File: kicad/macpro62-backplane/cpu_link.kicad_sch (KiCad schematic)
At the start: 0 parts

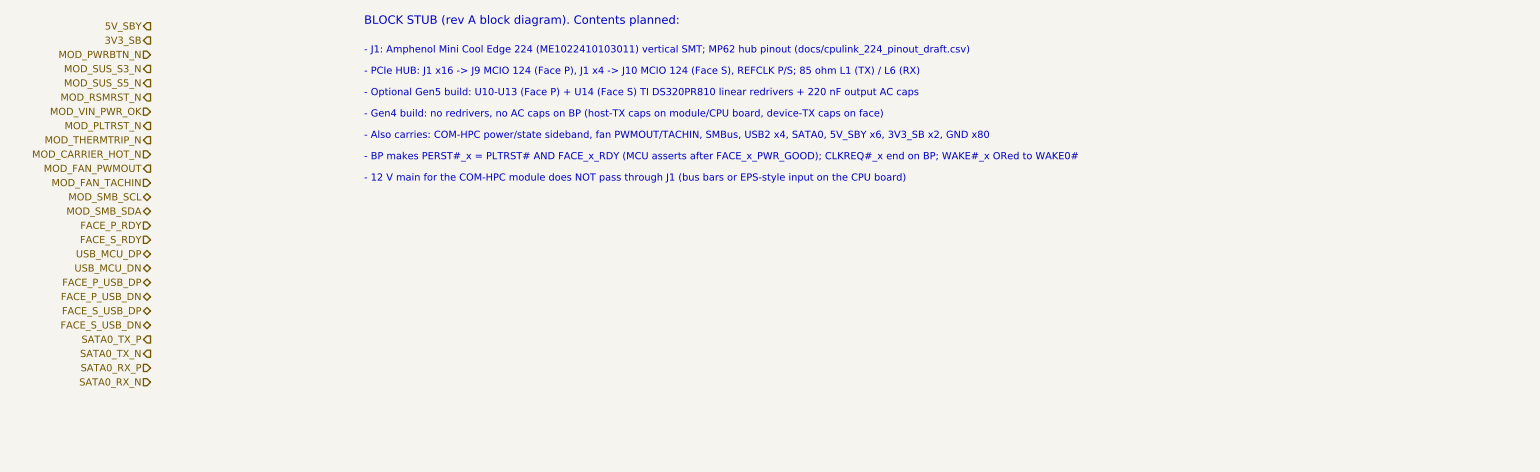
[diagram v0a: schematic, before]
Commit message: Cross-board compatibility audit: interface control doc, CR-BP-1 applied, J2/J3 row-swap pinouts, 15-pin face AUX, fan header removed from backplane, CPU board i226/BT1 cleanup
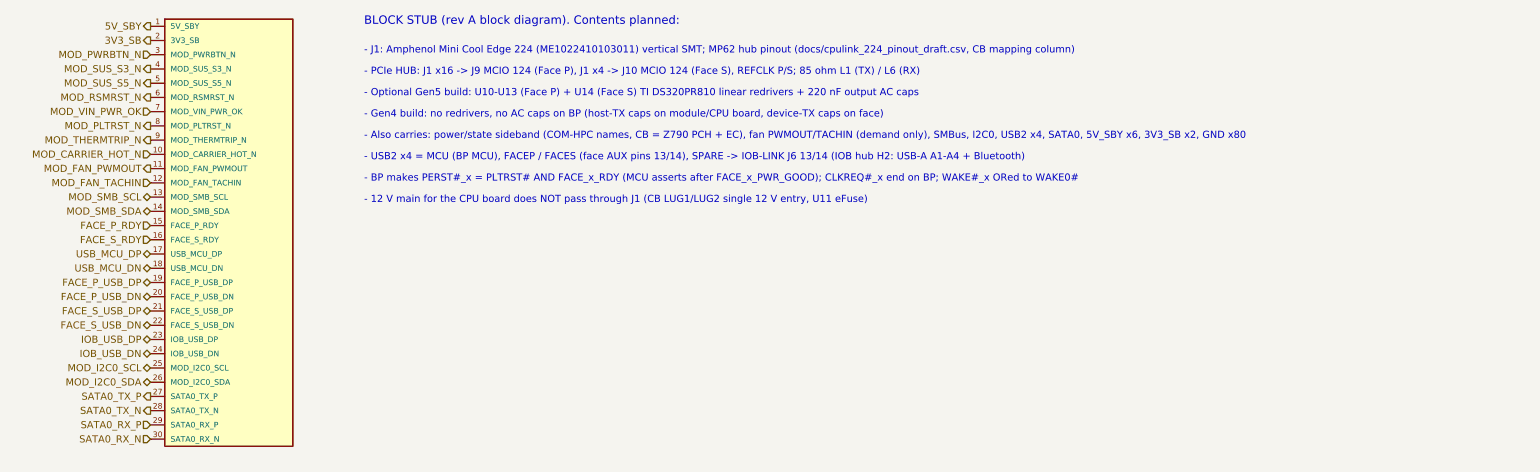
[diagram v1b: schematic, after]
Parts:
- added #BLK5: STUB_CPU_LINK, symbol MP62:STUB_CPU_LINK
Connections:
- net 3V3_SB: now also #BLK5.2 (3V3_SB)
- net 5V_SBY: now also #BLK5.1 (5V_SBY)
- net FACE_P_RDY: now also #BLK5.15 (FACE_P_RDY)
- net FACE_P_USB_DN: now also #BLK5.20 (FACE_P_USB_DN)
- net FACE_P_USB_DP: now also #BLK5.19 (FACE_P_USB_DP)
- net FACE_S_RDY: now also #BLK5.16 (FACE_S_RDY)
- net FACE_S_USB_DN: now also #BLK5.22 (FACE_S_USB_DN)
- net FACE_S_USB_DP: now also #BLK5.21 (FACE_S_USB_DP)
- net MOD_CARRIER_HOT_N: now also #BLK5.10 (MOD_CARRIER_HOT_N)
- net MOD_FAN_PWMOUT: now also #BLK5.11 (MOD_FAN_PWMOUT)
- net MOD_FAN_TACHIN: now also #BLK5.12 (MOD_FAN_TACHIN)
- net MOD_PLTRST_N: now also #BLK5.8 (MOD_PLTRST_N)
- net MOD_PWRBTN_N: now also #BLK5.3 (MOD_PWRBTN_N)
- net MOD_RSMRST_N: now also #BLK5.6 (MOD_RSMRST_N)
- net MOD_SMB_SCL: now also #BLK5.13 (MOD_SMB_SCL)
- net MOD_SMB_SDA: now also #BLK5.14 (MOD_SMB_SDA)
- net MOD_SUS_S3_N: now also #BLK5.4 (MOD_SUS_S3_N)
- net MOD_SUS_S5_N: now also #BLK5.5 (MOD_SUS_S5_N)
- net MOD_THERMTRIP_N: now also #BLK5.9 (MOD_THERMTRIP_N)
- net MOD_VIN_PWR_OK: now also #BLK5.7 (MOD_VIN_PWR_OK)
- net SATA0_RX_N: now also #BLK5.30 (SATA0_RX_N)
- net SATA0_RX_P: now also #BLK5.29 (SATA0_RX_P)
- net SATA0_TX_N: now also #BLK5.28 (SATA0_TX_N)
- net SATA0_TX_P: now also #BLK5.27 (SATA0_TX_P)
- net USB_MCU_DN: now also #BLK5.18 (USB_MCU_DN)
- net USB_MCU_DP: now also #BLK5.17 (USB_MCU_DP)
- new net IOB_USB_DN: #BLK5.24 (IOB_USB_DN)
- new net IOB_USB_DP: #BLK5.23 (IOB_USB_DP)
- new net MOD_I2C0_SCL: #BLK5.25 (MOD_I2C0_SCL)
- new net MOD_I2C0_SDA: #BLK5.26 (MOD_I2C0_SDA)
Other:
- note added: "- 12 V main for the CPU board does NOT pass through J1 (CB LUG1/LUG2 single 12 V entry, U11 eFuse)"
- note added: "- Also carries: power/state sideband (COM-HPC names, CB = Z790 PCH + EC), fan PWMOUT/TACHIN (demand only), SMBus, I2C0, USB2 x4, SATA0, 5V_SBY x6, 3V3_SB x2, GND x80"
- note added: "- J1: Amphenol Mini Cool Edge 224 (ME1022410103011) vertical SMT; MP62 hub pinout (docs/cpulink_224_pinout_draft.csv, CB mapping column)"
- note added: "- USB2 x4 = MCU (BP MCU), FACEP / FACES (face AUX pins 13/14), SPARE -> IOB-LINK J6 13/14 (IOB hub H2: USB-A A1-A4 + Bluetooth)"
- note removed: "- 12 V main for the COM-HPC module does NOT pass through J1 (bus bars or EPS-style input on the CPU board)"
- note removed: "- Also carries: COM-HPC power/state sideband, fan PWMOUT/TACHIN, SMBus, USB2 x4, SATA0, 5V_SBY x6, 3V3_SB x2, GND x80"
- note removed: "- J1: Amphenol Mini Cool Edge 224 (ME1022410103011) vertical SMT; MP62 hub pinout (docs/cpulink_224_pinout_draft.csv)"
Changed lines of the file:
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@@
 	(title_block
 		(title "MP62 backplane: CPU board link (J1 CPU-LINK card edge)")
-		(date "2026-10-01")
-		(rev "A-bd1")
-		(comment 1 "Block stub: hierarchical labels only, circuit TBD")
+		(date "2026-10-02")
+		(rev "A-bd2")
+		(comment 1 "Block stub: hierarchical labels + one non-BOM stub symbol (#BLKn, passive pins) so ERC sees the nets; circuit TBD")
 	)
 	(hierarchical_label "5V_SBY"
@@
 		(effects (font (size 1.27 1.27)) (justify right))
 	)
+	(hierarchical_label "IOB_USB_DP"
+		(shape bidirectional)
+		(at 38.1 86.36 180)
+		(effects (font (size 1.27 1.27)) (justify right))
+	)
+	(hierarchical_label "IOB_USB_DN"
+		(shape bidirectional)
+		(at 38.1 88.90 180)
+		(effects (font (size 1.27 1.27)) (justify right))
+	)
+	(hierarchical_label "MOD_I2C0_SCL"
+		(shape bidirectional)
+		(at 38.1 91.44 180)
+		(effects (font (size 1.27 1.27)) (justify right))
+	)
+	(hierarchical_label "MOD_I2C0_SDA"
+		(shape bidirectional)
+		(at 38.1 93.98 180)
+		(effects (font (size 1.27 1.27)) (justify right))
+	)
 	(hierarchical_label "SATA0_TX_P"
 		(shape output)
-		(at 38.1 86.36 180)
+		(at 38.1 96.52 180)
 		(effects (font (size 1.27 1.27)) (justify right))
 	)
 	(hierarchical_label "SATA0_TX_N"
 		(shape output)
-		(at 38.1 88.90 180)
+		(at 38.1 99.06 180)
 		(effects (font (size 1.27 1.27)) (justify right))
 	)
 	(hierarchical_label "SATA0_RX_P"
 		(shape input)
-		(at 38.1 91.44 180)
+		(at 38.1 101.60 180)
 		(effects (font (size 1.27 1.27)) (justify right))
 	)
 	(hierarchical_label "SATA0_RX_N"
 		(shape input)
-		(at 38.1 93.98 180)
-		(effects (font (size 1.27 1.27)) (justify right))
+		(at 38.1 104.14 180)
+		(effects (font (size 1.27 1.27)) (justify right))
+	)
+	(symbol
+		(lib_id "MP62:STUB_CPU_LINK")
+		(at 38.1 30.48 0)
+		(unit 1)
+		(exclude_from_sim yes)
+		(in_bom no)
+		(on_board no)
+		(dnp no)
+		(property "Reference" "#BLK5"
+			(at 40.64 27.94 0)
+			(effects (font (size 1.27 1.27)) (justify left) (hide yes))
+		)
+		(property "Value" "STUB_CPU_LINK"
+			(at 40.64 26.67 0)
+			(effects (font (size 1.27 1.27)) (justify left) (hide yes))
+		)
+		(pin "1"
+		)
+		(pin "2"
+		)
+		(pin "3"
+		)
+		(pin "4"
+		)
+		(pin "5"
+		)
+		(pin "6"
+		)
+		(pin "7"
+		)
+		(pin "8"
+		)
+		(pin "9"
+		)
+		(pin "10"
+		)
+		(pin "11"
+		)
+		(pin "12"
+		)
+		(pin "13"
+		)
+		(pin "14"
+		)
+		(pin "15"
+		)
+		(pin "16"
+		)
+		(pin "17"
+		)
+		(pin "18"
+		)
+		(pin "19"
+		)
+		(pin "20"
+		)
+		(pin "21"
+		)
+		(pin "22"
+		)
+		(pin "23"
+		)
+		(pin "24"
+		)
+		(pin "25"
+		)
+		(pin "26"
+		)
+		(pin "27"
+		)
+		(pin "28"
+		)
+		(pin "29"
+		)
+		(pin "30"
+		)
+		(instances
+			(project "backplane"
+				(path "/6a1c2d3e-0000-4000-8000-000000000062/f1a0d997-9be8-4b41-9317-5f875cd4202e"
+					(reference "#BLK5")
+					(unit 1)
+				)
+			)
+		)
 	)
 	(text "BLOCK STUB (rev A block diagram). Contents planned:"
@@
 		(effects (font (size 1.5 1.5)) (justify left bottom))
 	)
-	(text "- J1: Amphenol Mini Cool Edge 224 (ME1022410103011) vertical SMT; MP62 hub pinout (docs/cpulink_224_pinout_draft.csv)"
+	(text "- J1: Amphenol Mini Cool Edge 224 (ME1022410103011) vertical SMT; MP62 hub pinout (docs/cpulink_224_pinout_draft.csv, CB mapping column)"
 		(exclude_from_sim no)
 		(at 76.20 35.56 0)
@@
 		(effects (font (size 1.27 1.27)) (justify left bottom))
 	)
-	(text "- Also carries: COM-HPC power/state sideband, fan PWMOUT/TACHIN, SMBus, USB2 x4, SATA0, 5V_SBY x6, 3V3_SB x2, GND x80"
+	(text "- Also carries: power/state sideband (COM-HPC names, CB = Z790 PCH + EC), fan PWMOUT/TACHIN (demand only), SMBus, I2C0, USB2 x4, SATA0, 5V_SBY x6, 3V3_SB x2, GND x80"
 		(exclude_from_sim no)
 		(at 76.20 50.80 0)
 		(effects (font (size 1.27 1.27)) (justify left bottom))
 	)
+	(text "- USB2 x4 = MCU (BP MCU), FACEP / FACES (face AUX pins 13/14), SPARE -> IOB-LINK J6 13/14 (IOB hub H2: USB-A A1-A4 + Bluetooth)"
+		(exclude_from_sim no)
+		(at 76.20 54.61 0)
+		(effects (font (size 1.27 1.27)) (justify left bottom))
+	)
 	(text "- BP makes PERST#_x = PLTRST# AND FACE_x_RDY (MCU asserts after FACE_x_PWR_GOOD); CLKREQ#_x end on BP; WAKE#_x ORed to WAKE0#"
 		(exclude_from_sim no)
-		(at 76.20 54.61 0)
-		(effects (font (size 1.27 1.27)) (justify left bottom))
-	)
-	(text "- 12 V main for the COM-HPC module does NOT pass through J1 (bus bars or EPS-style input on the CPU board)"
-		(exclude_from_sim no)
 		(at 76.20 58.42 0)
 		(effects (font (size 1.27 1.27)) (justify left bottom))
 	)
+	(text "- 12 V main for the CPU board does NOT pass through J1 (CB LUG1/LUG2 single 12 V entry, U11 eFuse)"
+		(exclude_from_sim no)
+		(at 76.20 62.23 0)
+		(effects (font (size 1.27 1.27)) (justify left bottom))
+	)

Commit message: ICD rev 2: 45 deg faces, 445 W ceiling + live power target (INA228 telemetry), ribbon MCIO jog cables, BT on S0, fan fail-safe, port-module I2C map
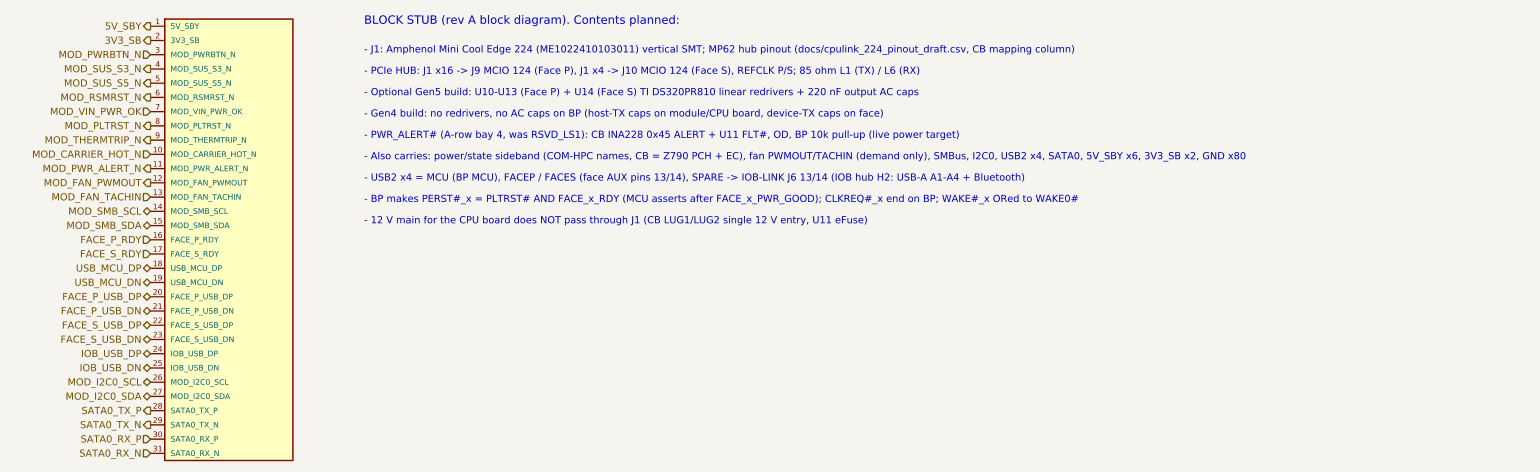
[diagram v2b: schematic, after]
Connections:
- net FACE_P_RDY: now also #BLK5.16 (FACE_P_RDY); no longer #BLK5.15 (FACE_P_RDY)
- net FACE_P_USB_DN: now also #BLK5.21 (FACE_P_USB_DN); no longer #BLK5.20 (FACE_P_USB_DN)
- net FACE_P_USB_DP: now also #BLK5.20 (FACE_P_USB_DP); no longer #BLK5.19 (FACE_P_USB_DP)
- net FACE_S_RDY: now also #BLK5.17 (FACE_S_RDY); no longer #BLK5.16 (FACE_S_RDY)
- net FACE_S_USB_DN: now also #BLK5.23 (FACE_S_USB_DN); no longer #BLK5.22 (FACE_S_USB_DN)
- net FACE_S_USB_DP: now also #BLK5.22 (FACE_S_USB_DP); no longer #BLK5.21 (FACE_S_USB_DP)
- net IOB_USB_DN: now also #BLK5.25 (IOB_USB_DN); no longer #BLK5.24 (IOB_USB_DN)
- net IOB_USB_DP: now also #BLK5.24 (IOB_USB_DP); no longer #BLK5.23 (IOB_USB_DP)
- net MOD_FAN_PWMOUT: now also #BLK5.12 (MOD_FAN_PWMOUT); no longer #BLK5.11 (MOD_FAN_PWMOUT)
- net MOD_FAN_TACHIN: now also #BLK5.13 (MOD_FAN_TACHIN); no longer #BLK5.12 (MOD_FAN_TACHIN)
- net MOD_I2C0_SCL: now also #BLK5.26 (MOD_I2C0_SCL); no longer #BLK5.25 (MOD_I2C0_SCL)
- net MOD_I2C0_SDA: now also #BLK5.27 (MOD_I2C0_SDA); no longer #BLK5.26 (MOD_I2C0_SDA)
- net MOD_SMB_SCL: now also #BLK5.14 (MOD_SMB_SCL); no longer #BLK5.13 (MOD_SMB_SCL)
- net MOD_SMB_SDA: now also #BLK5.15 (MOD_SMB_SDA); no longer #BLK5.14 (MOD_SMB_SDA)
- net SATA0_RX_N: now also #BLK5.31 (SATA0_RX_N); no longer #BLK5.30 (SATA0_RX_N)
- net SATA0_RX_P: now also #BLK5.30 (SATA0_RX_P); no longer #BLK5.29 (SATA0_RX_P)
- net SATA0_TX_N: now also #BLK5.29 (SATA0_TX_N); no longer #BLK5.28 (SATA0_TX_N)
- net SATA0_TX_P: now also #BLK5.28 (SATA0_TX_P); no longer #BLK5.27 (SATA0_TX_P)
- net USB_MCU_DN: now also #BLK5.19 (USB_MCU_DN); no longer #BLK5.18 (USB_MCU_DN)
- net USB_MCU_DP: now also #BLK5.18 (USB_MCU_DP); no longer #BLK5.17 (USB_MCU_DP)
- new net MOD_PWR_ALERT_N: #BLK5.11 (MOD_PWR_ALERT_N)
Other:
- note added: "- PWR_ALERT# (A-row bay 4, was RSVD_LS1): CB INA228 0x45 ALERT + U11 FLT#, OD, BP 10k pull-up (live power target)"
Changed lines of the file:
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@@
+		(effects (font (size 1.27 1.27)) (justify right))
+	)
+	(hierarchical_label "MOD_PWR_ALERT_N"
+		(shape output)
+		(at 38.1 55.88 180)
 		(effects (font (size 1.27 1.27)) (justify right))
 	)
 	(hierarchical_label "MOD_FAN_PWMOUT"
 		(shape output)
-		(at 38.1 55.88 180)
+		(at 38.1 58.42 180)
 		(effects (font (size 1.27 1.27)) (justify right))
 	)
 	(hierarchical_label "MOD_FAN_TACHIN"
 		(shape input)
-		(at 38.1 58.42 180)
+		(at 38.1 60.96 180)
 		(effects (font (size 1.27 1.27)) (justify right))
 	)
 	(hierarchical_label "MOD_SMB_SCL"
 		(shape bidirectional)
-		(at 38.1 60.96 180)
+		(at 38.1 63.50 180)
 		(effects (font (size 1.27 1.27)) (justify right))
 	)
 	(hierarchical_label "MOD_SMB_SDA"
 		(shape bidirectional)
-		(at 38.1 63.50 180)
+		(at 38.1 66.04 180)
 		(effects (font (size 1.27 1.27)) (justify right))
 	)
 	(hierarchical_label "FACE_P_RDY"
 		(shape input)
-		(at 38.1 66.04 180)
+		(at 38.1 68.58 180)
 		(effects (font (size 1.27 1.27)) (justify right))
 	)
 	(hierarchical_label "FACE_S_RDY"
 		(shape input)
-		(at 38.1 68.58 180)
+		(at 38.1 71.12 180)
 		(effects (font (size 1.27 1.27)) (justify right))
 	)
 	(hierarchical_label "USB_MCU_DP"
 		(shape bidirectional)
-		(at 38.1 71.12 180)
+		(at 38.1 73.66 180)
 		(effects (font (size 1.27 1.27)) (justify right))
 	)
 	(hierarchical_label "USB_MCU_DN"
 		(shape bidirectional)
-		(at 38.1 73.66 180)
+		(at 38.1 76.20 180)
 		(effects (font (size 1.27 1.27)) (justify right))
 	)
 	(hierarchical_label "FACE_P_USB_DP"
 		(shape bidirectional)
-		(at 38.1 76.20 180)
+		(at 38.1 78.74 180)
 		(effects (font (size 1.27 1.27)) (justify right))
 	)
 	(hierarchical_label "FACE_P_USB_DN"
 		(shape bidirectional)
-		(at 38.1 78.74 180)
+		(at 38.1 81.28 180)
 		(effects (font (size 1.27 1.27)) (justify right))
 	)
 	(hierarchical_label "FACE_S_USB_DP"
 		(shape bidirectional)
-		(at 38.1 81.28 180)
+		(at 38.1 83.82 180)
 		(effects (font (size 1.27 1.27)) (justify right))
 	)
 	(hierarchical_label "FACE_S_USB_DN"
 		(shape bidirectional)
-		(at 38.1 83.82 180)
+		(at 38.1 86.36 180)
 		(effects (font (size 1.27 1.27)) (justify right))
 	)
 	(hierarchical_label "IOB_USB_DP"
 		(shape bidirectional)
-		(at 38.1 86.36 180)
+		(at 38.1 88.90 180)
 		(effects (font (size 1.27 1.27)) (justify right))
 	)
 	(hierarchical_label "IOB_USB_DN"
 		(shape bidirectional)
-		(at 38.1 88.90 180)
+		(at 38.1 91.44 180)
 		(effects (font (size 1.27 1.27)) (justify right))
 	)
 	(hierarchical_label "MOD_I2C0_SCL"
 		(shape bidirectional)
-		(at 38.1 91.44 180)
+		(at 38.1 93.98 180)
 		(effects (font (size 1.27 1.27)) (justify right))
 	)
 	(hierarchical_label "MOD_I2C0_SDA"
 		(shape bidirectional)
-		(at 38.1 93.98 180)
+		(at 38.1 96.52 180)
 		(effects (font (size 1.27 1.27)) (justify right))
 	)
 	(hierarchical_label "SATA0_TX_P"
 		(shape output)
-		(at 38.1 96.52 180)
+		(at 38.1 99.06 180)
 		(effects (font (size 1.27 1.27)) (justify right))
 	)
 	(hierarchical_label "SATA0_TX_N"
 		(shape output)
-		(at 38.1 99.06 180)
+		(at 38.1 101.60 180)
 		(effects (font (size 1.27 1.27)) (justify right))
 	)
 	(hierarchical_label "SATA0_RX_P"
 		(shape input)
-		(at 38.1 101.60 180)
+		(at 38.1 104.14 180)
 		(effects (font (size 1.27 1.27)) (justify right))
 	)
 	(hierarchical_label "SATA0_RX_N"
 		(shape input)
-		(at 38.1 104.14 180)
+		(at 38.1 106.68 180)
 		(effects (font (size 1.27 1.27)) (justify right))
 	)
@@
 		(pin "30"
 		)
+		(pin "31"
+		)
 		(instances
 			(project "backplane"
-				(path "/6a1c2d3e-0000-4000-8000-000000000062/f1a0d997-9be8-4b41-9317-5f875cd4202e"
+				(path "/6a1c2d3e-0000-4000-8000-000000000062/f910959d-2921-4c44-846a-6e33bd56610d"
 					(reference "#BLK5")
 					(unit 1)
@@
 		(effects (font (size 1.27 1.27)) (justify left bottom))
 	)
+	(text "- PWR_ALERT# (A-row bay 4, was RSVD_LS1): CB INA228 0x45 ALERT + U11 FLT#, OD, BP 10k pull-up (live power target)"
+		(exclude_from_sim no)
+		(at 76.20 50.80 0)
+		(effects (font (size 1.27 1.27)) (justify left bottom))
+	)
 	(text "- Also carries: power/state sideband (COM-HPC names, CB = Z790 PCH + EC), fan PWMOUT/TACHIN (demand only), SMBus, I2C0, USB2 x4, SATA0, 5V_SBY x6, 3V3_SB x2, GND x80"
 		(exclude_from_sim no)
-		(at 76.20 50.80 0)
+		(at 76.20 54.61 0)
 		(effects (font (size 1.27 1.27)) (justify left bottom))
 	)
 	(text "- USB2 x4 = MCU (BP MCU), FACEP / FACES (face AUX pins 13/14), SPARE -> IOB-LINK J6 13/14 (IOB hub H2: USB-A A1-A4 + Bluetooth)"
 		(exclude_from_sim no)
-		(at 76.20 54.61 0)
+		(at 76.20 58.42 0)
 		(effects (font (size 1.27 1.27)) (justify left bottom))
 	)
 	(text "- BP makes PERST#_x = PLTRST# AND FACE_x_RDY (MCU asserts after FACE_x_PWR_GOOD); CLKREQ#_x end on BP; WAKE#_x ORed to WAKE0#"
 		(exclude_from_sim no)
-		(at 76.20 58.42 0)
+		(at 76.20 62.23 0)
 		(effects (font (size 1.27 1.27)) (justify left bottom))
 	)
 	(text "- 12 V main for the CPU board does NOT pass through J1 (CB LUG1/LUG2 single 12 V entry, U11 eFuse)"
 		(exclude_from_sim no)
-		(at 76.20 62.23 0)
-		(effects (font (size 1.27 1.27)) (justify left bottom))
-	)
+		(at 76.20 66.04 0)
+		(effects (font (size 1.27 1.27)) (justify left bottom))
+	)
